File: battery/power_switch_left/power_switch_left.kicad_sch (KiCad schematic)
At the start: 1 part

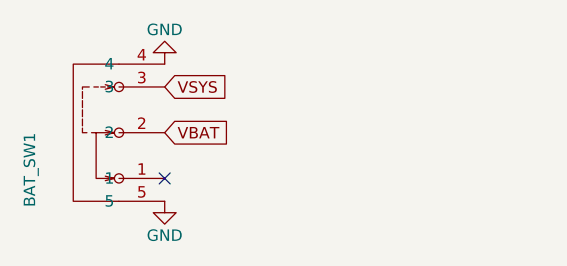
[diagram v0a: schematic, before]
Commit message: use SK12D07VG5
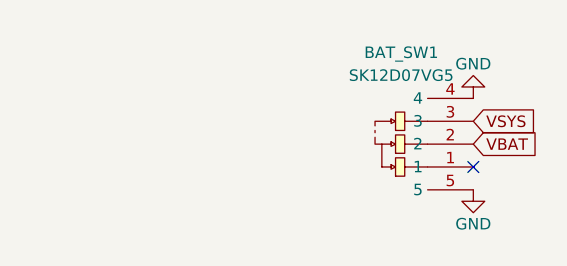
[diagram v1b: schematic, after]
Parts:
- removed BAT_SW1: ~, ErgoCai.pretty:SW-TH_SK12D07VG4, symbol ErgoCai:SK12D07VG4
- added BAT_SW1: SK12D07VG5, ErgoCai.pretty:SW-TH_SK12D07VG5-1, symbol ErgoCai:SK12D07VG5
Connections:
- net GND: now also BAT_SW1.4, BAT_SW1.5
- net VBAT: now also BAT_SW1.2
- net VSYS: now also BAT_SW1.3
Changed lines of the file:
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@@
 	(paper "A4")
 	(no_connect
-		(at 86.36 78.74)
+		(at 120.65 77.47)
 	)
 	(global_label "VSYS"
 		(shape input)
-		(at 86.36 68.58 0)
+		(at 120.65 72.39 0)
 		(fields_autoplaced yes)
 		(effects
@@
 		)
 		(property "Intersheetrefs" "${INTERSHEET_REFS}"
-			(at 93.9414 68.58 0)
+			(at 128.2314 72.39 0)
 			(effects
 				(font
@@
 	(global_label "VBAT"
 		(shape input)
-		(at 86.36 73.66 0)
+		(at 120.65 74.93 0)
 		(fields_autoplaced yes)
 		(effects
@@
 		)
 		(property "Intersheetrefs" "${INTERSHEET_REFS}"
-			(at 93.76 73.66 0)
+			(at 128.05 74.93 0)
 			(effects
 				(font
@@
 	)
 	(symbol
-		(lib_id "ErgoCai:SK12D07VG4")
-		(at 81.28 73.66 90)
+		(lib_id "ErgoCai:SK12D07VG5")
+		(at 115.57 74.93 90)
 		(unit 1)
 		(exclude_from_sim no)
@@
 		(on_board yes)
 		(dnp no)
+		(fields_autoplaced yes)
 		(property "Reference" "BAT_SW1"
-			(at 71.374 73.66 0)
-			(effects
-				(font
-					(size 1.27 1.27)
-				)
-				(justify right)
-			)
-		)
-		(property "Value" "~"
-			(at 78.7401 80.01 0)
-			(effects
-				(font
-					(size 1.27 1.27)
-				)
-				(justify right)
-			)
-		)
-		(property "Footprint" "ErgoCai.pretty:SW-TH_SK12D07VG4"
-			(at 81.28 73.66 0)
-			(effects
-				(font
-					(size 1.27 1.27)
-				)
-				(justify bottom)
-				(hide yes)
-			)
-		)
-		(property "Datasheet" "https://lcsc.com/product-detail/Toggle-Switches_SHOU-HAN-SK12D07VG4_C393937.html"
-			(at 81.28 73.66 0)
-			(effects
-				(font
-					(size 1.27 1.27)
-				)
-				(hide yes)
-			)
-		)
-		(property "Description" "Switch, dual pole double throw, separate symbols"
-			(at 81.28 73.66 0)
-			(effects
-				(font
-					(size 1.27 1.27)
-				)
-				(hide yes)
-			)
-		)
-		(property "MF" "C&K"
-			(at 81.28 73.66 0)
-			(effects
-				(font
-					(size 1.27 1.27)
-				)
-				(justify bottom)
-				(hide yes)
-			)
-		)
-		(property "Description_1" "Switch Slide ON ON SPDT Side Slide 0.3A 30VDC PC Pins Bracket Mount/Through Hole Bulk"
-			(at 81.28 73.66 0)
-			(effects
-				(font
-					(size 1.27 1.27)
-				)
-				(justify bottom)
-				(hide yes)
-			)
-		)
-		(property "Package" "None"
-			(at 81.28 73.66 0)
-			(effects
-				(font
-					(size 1.27 1.27)
-				)
-				(justify bottom)
-				(hide yes)
-			)
-		)
-		(property "Price" "None"
-			(at 81.28 73.66 0)
-			(effects
-				(font
-					(size 1.27 1.27)
-				)
-				(justify bottom)
-				(hide yes)
-			)
-		)
-		(property "SnapEDA_Link" "https://www.snapeda.com/parts/SK12D07VG4/C%2526K/view-part/?ref=snap"
-			(at 81.28 73.66 0)
-			(effects
-				(font
-					(size 1.27 1.27)
-				)
-				(justify bottom)
-				(hide yes)
-			)
-		)
-		(property "MP" "SK12D07VG4"
-			(at 81.28 73.66 0)
-			(effects
-				(font
-					(size 1.27 1.27)
-				)
-				(justify bottom)
-				(hide yes)
-			)
-		)
-		(property "Availability" "Not in stock"
-			(at 81.28 73.66 0)
-			(effects
-				(font
-					(size 1.27 1.27)
-				)
-				(justify bottom)
-				(hide yes)
-			)
-		)
-		(property "Check_prices" "https://www.snapeda.com/parts/SK12D07VG4/C%2526K/view-part/?ref=eda"
-			(at 81.28 73.66 0)
-			(effects
-				(font
-					(size 1.27 1.27)
-				)
-				(justify bottom)
-				(hide yes)
-			)
-		)
-		(property "LCSC Part" "C393937"
-			(at 99.06 73.66 0)
-			(effects
-				(font
-					(size 1.27 1.27)
-				)
-				(hide yes)
-			)
+			(at 112.65 64.77 90)
+			(effects
+				(font
+					(size 1.27 1.27)
+				)
+			)
+		)
+		(property "Value" "SK12D07VG5"
+			(at 112.65 67.31 90)
+			(effects
+				(font
+					(size 1.27 1.27)
+				)
+			)
+		)
+		(property "Footprint" "ErgoCai.pretty:SW-TH_SK12D07VG5-1"
+			(at 128.27 74.93 0)
+			(effects
+				(font
+					(size 1.27 1.27)
+				)
+				(hide yes)
+			)
+		)
+		(property "Datasheet" "https://lcsc.com/product-detail/Toggle-Switches_SHOU-HAN-SK12D07VG5_C431548.html"
+			(at 130.81 74.93 0)
+			(effects
+				(font
+					(size 1.27 1.27)
+				)
+				(hide yes)
+			)
+		)
+		(property "Description" ""
+			(at 115.57 74.93 0)
+			(effects
+				(font
+					(size 1.27 1.27)
+				)
+				(hide yes)
+			)
+		)
+		(property "LCSC Part" "C431548"
+			(at 133.35 74.93 0)
+			(effects
+				(font
+					(size 1.27 1.27)
+				)
+				(hide yes)
+			)
+		)
+		(pin "2"
+		)
+		(pin "1"
 		)
 		(pin "5"
 		)
-		(pin "2"
-		)
-		(pin "1"
+		(pin "4"
 		)
 		(pin "3"
 		)
-		(pin "4"
-		)
 		(instances
-			(project "power_switch_left"
+			(project ""
 				(path "/0b983ce8-f198-41fe-b960-fba89418c139"
 					(reference "BAT_SW1")
@@
 	(symbol
 		(lib_id "power:GND")
-		(at 86.36 81.28 0)
+		(at 120.65 80.01 0)
 		(unit 1)
 		(exclude_from_sim no)
@@
 		(dnp no)
 		(property "Reference" "#PWR01"
-			(at 86.36 87.63 0)
+			(at 120.65 86.36 0)
 			(effects
 				(font
@@
 		)
 		(property "Value" "GND"
-			(at 86.36 85.09 0)
+			(at 120.65 83.82 0)
 			(effects
 				(font
@@
 		)
 		(property "Footprint" ""
-			(at 86.36 81.28 0)
+			(at 120.65 80.01 0)
 			(effects
 				(font
@@
 		)
 		(property "Datasheet" ""
-			(at 86.36 81.28 0)
+			(at 120.65 80.01 0)
 			(effects
 				(font
@@
 		)
 		(property "Description" "Power symbol creates a global label with name \"GND\" , ground"
-			(at 86.36 81.28 0)
+			(at 120.65 80.01 0)
 			(effects
 				(font
@@
 	(symbol
 		(lib_id "power:GND")
-		(at 86.36 66.04 180)
+		(at 120.65 69.85 180)
 		(unit 1)
 		(exclude_from_sim no)
@@
 		(dnp no)
 		(property "Reference" "#PWR03"
-			(at 86.36 59.69 0)
+			(at 120.65 63.5 0)
 			(effects
 				(font
@@
 		)
 		(property "Value" "GND"
-			(at 86.36 62.23 0)
+			(at 120.65 66.04 0)
 			(effects
 				(font
@@
 		)
 		(property "Footprint" ""
-			(at 86.36 66.04 0)
+			(at 120.65 69.85 0)
 			(effects
 				(font
@@
 		)
 		(property "Datasheet" ""
-			(at 86.36 66.04 0)
+			(at 120.65 69.85 0)
 			(effects
 				(font
@@
 		)
 		(property "Description" "Power symbol creates a global label with name \"GND\" , ground"
-			(at 86.36 66.04 0)
-			(effects
-				(font
+			(at 120.65 69.85 0)
+			(effects
+				(font

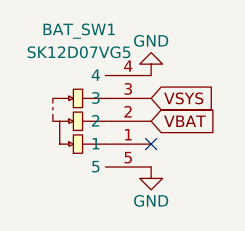
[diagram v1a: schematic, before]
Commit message: update power switch
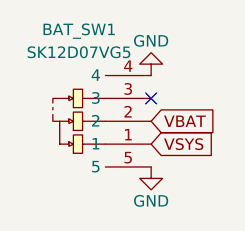
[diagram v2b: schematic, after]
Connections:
- net VSYS: now also BAT_SW1.1; no longer BAT_SW1.3
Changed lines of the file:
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@@
 	(paper "A4")
 	(no_connect
-		(at 120.65 77.47)
+		(at 120.65 72.39)
 	)
 	(global_label "VSYS"
 		(shape input)
-		(at 120.65 72.39 0)
+		(at 120.65 77.47 0)
 		(fields_autoplaced yes)
 		(effects
@@
 		)
 		(property "Intersheetrefs" "${INTERSHEET_REFS}"
-			(at 128.2314 72.39 0)
+			(at 128.2314 77.47 0)
 			(effects
 				(font
@@
 		)
 		(instances
-			(project ""
+			(project "power_switch_left"
 				(path "/0b983ce8-f198-41fe-b960-fba89418c139"
 					(reference "BAT_SW1")
